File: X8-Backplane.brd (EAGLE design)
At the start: 122.1 x 89 mm, 18 parts, among them U1 BD6221FSOP, U2 MIC29501-5.0WU, U3 MIC29501-5.0WU, U4 FQB27P06, U5 FQB27P06, U6 FQB27P06

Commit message: added buck regulator
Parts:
- removed C1, C7: 10uF, SparkFun-Passives:0603-CAP
- removed C5, C8: 0.1uF, SparkFun-Passives:0603-CAP
- removed R1, R2: 10k, SparkFun-Passives:0603-RES
- removed U2, U3: MIC29501-5.0WU, LDO:TO-263-5
- added C10, C6, C9: 150uF, PowerComponents:CTAN(7.30_4.30MM)
- added C11, C12, C13, C2: 10uF, PowerComponents:CTAN(7.30_4.30MM)
- added C3: 0.47uF, SparkFun-Capacitors:0805
- added C4: 0.01uF, SparkFun-Passives:0603-CAP
- added U$2: SWITCHMODE_SCHOTTKY, PowerComponents:DPAK-3
- added U$6: 15uH, DiscreteComponents:HCMA1305
- added U7: LM2678, PowerComponents:LM2678
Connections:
- removed net +5V_CAMERA_TUBE: C7.1, U$4.57, U$4.58, U$4.59, U$4.60, U3.4, U4.3, U5.3, U6.3
- removed net EN1: R1.1, U2.1
- removed net EN2: R2.1, U3.1
- new net N$18: C4.1, U7.3
- new net N$19: C4.2, U$2.P$4, U$6.P$1, U7.1
- net +12V: now also C11.+, C12.+, C13.+, C2.+, C3.1, U7.2; no longer C5.1, C8.1, R1.2, R2.2, U2.2, U3.2
- net +5V: now also C10.+, C6.+, C9.+, U$4.57, U$4.58, U$4.59, U$4.60, U$6.P$2, U4.3, U5.3, U6.3, U7.6; no longer C1.1, U2.4
- net GND: now also C10.-, C11.-, C12.-, C13.-, C2.-, C3.2, C6.-, C9.-, U$2.P$1, U$2.P$3, U7.4, U7.TAB; no longer C1.2, C5.2, C7.2, C8.2, U2.3, U2.6, U3.3, U3.6
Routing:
- net +5V_LASER: track 0.00 -> 46.4 mm
- net +5V: track 108.6 -> 94.8 mm, vias 0 -> 2
- net N$19: track 0.00 -> 4.33 mm, vias 0 -> 1
- net N$18: track 0.00 -> 3.85 mm, vias 0 -> 1
- net +12V: track 2.52 -> 0.00 mm
- net EN1: track 2.01 -> 0.00 mm
- net EN2: track 1.93 -> 0.00 mm
- added copper zone on layer 16, net +5V
- added copper zone on layer 16, net N$19
- removed copper zone on layer 16, net +5V_CAMERA_TUBE
- removed copper zone on layer 16, net +5V_LASER

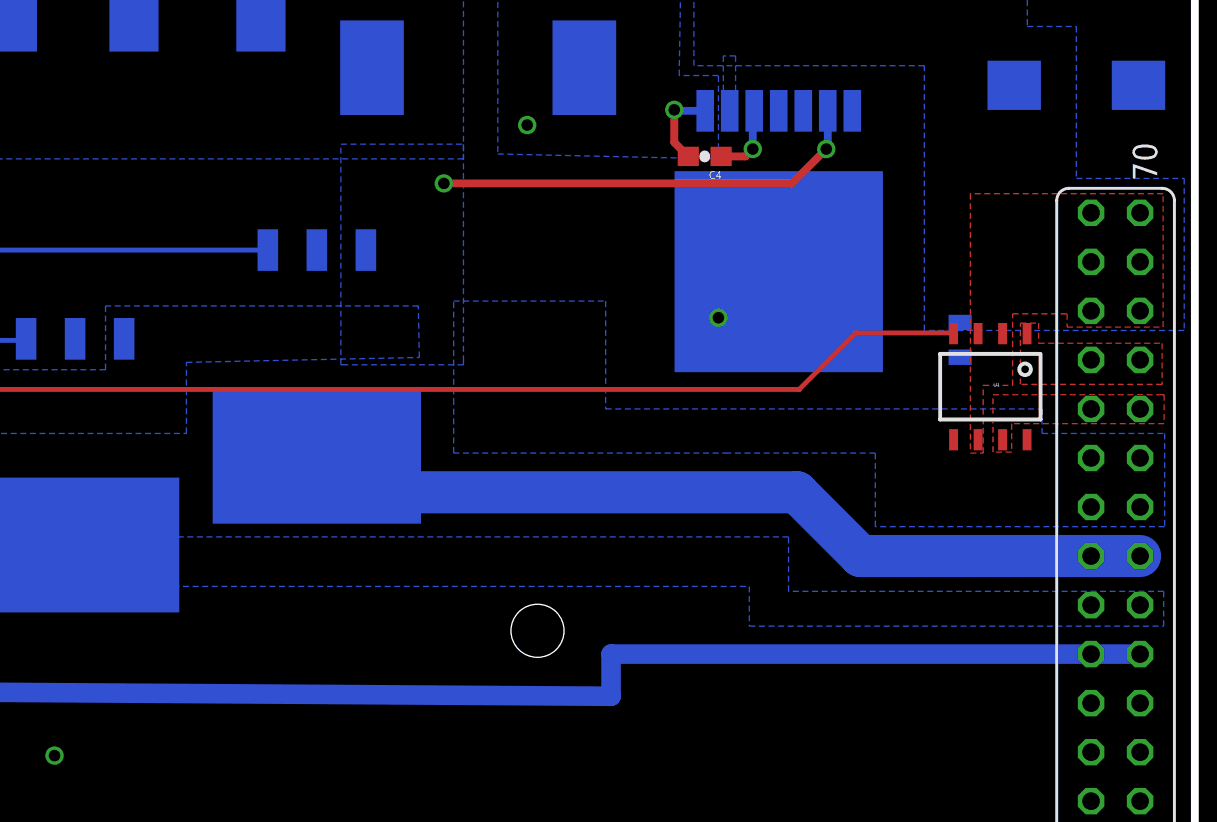
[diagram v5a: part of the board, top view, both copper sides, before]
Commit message: added more gnd vias
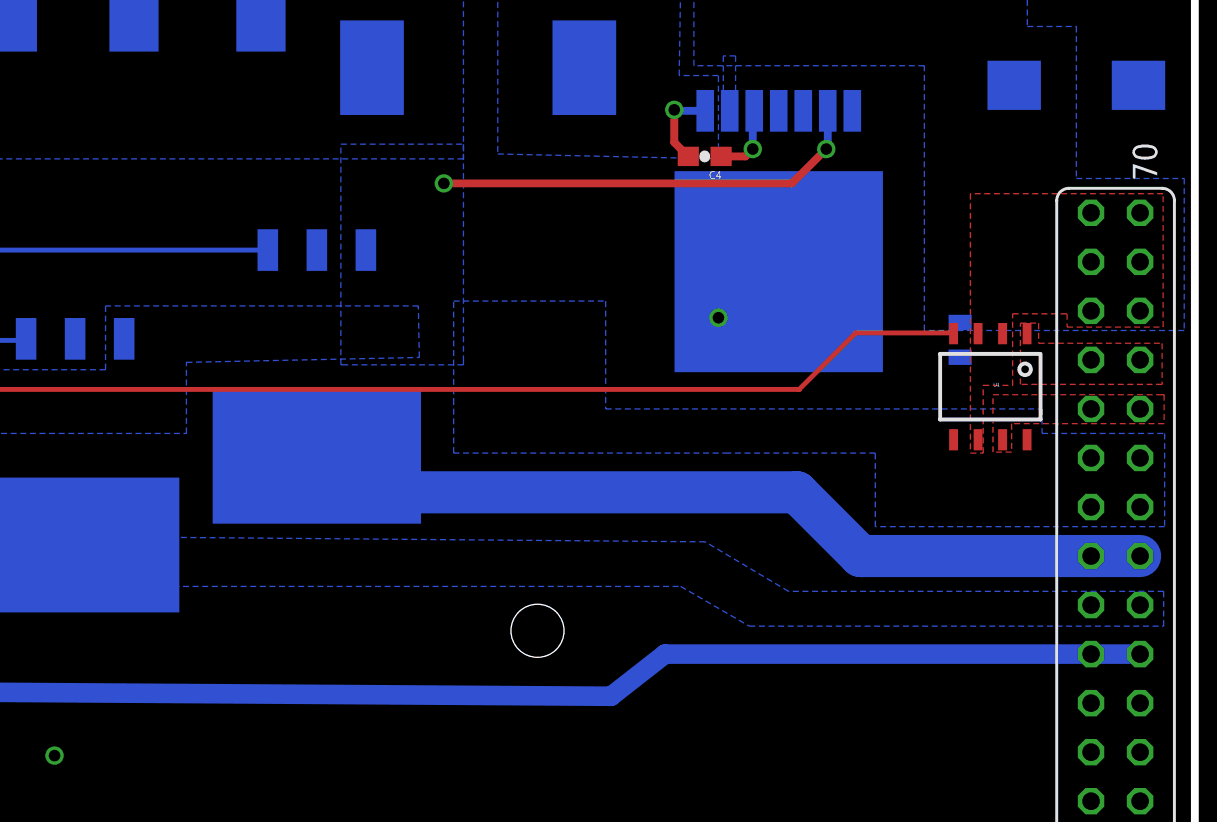
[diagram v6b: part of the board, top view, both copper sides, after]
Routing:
- net +5V_BT_LED: track 71.2 -> 69.7 mm
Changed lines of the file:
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@@
 <grid distance="10" unitdist="mil" unit="mil" style="lines" multiple="1" display="yes" altdistance="0.001" altunitdist="inch" altunit="inch"/>
 <layers>
-<layer number="1" name="Top" color="4" fill="1" visible="no" active="yes"/>
+<layer number="1" name="Top" color="4" fill="1" visible="yes" active="yes"/>
 <layer number="2" name="Route2" color="1" fill="3" visible="yes" active="yes"/>
 <layer number="3" name="Route3" color="4" fill="3" visible="no" active="yes"/>
@@
 <via x="47.1678" y="81.7626" extent="1-16" drill="0.6" diameter="0.3048"/>
 <via x="22.4028" y="64.0334" extent="1-16" drill="0.6" diameter="0.3048"/>
+<via x="32.385" y="35.433" extent="1-16" drill="0.6" diameter="0.3048"/>
+<via x="65.4304" y="21.6662" extent="1-16" drill="0.6" diameter="0.3048"/>
+<via x="102.9462" y="12.0396" extent="1-16" drill="0.6" diameter="0.3048"/>
+<via x="53.2638" y="57.9374" extent="1-16" drill="0.6" diameter="0.3048"/>
+<via x="49.2252" y="66.3194" extent="1-16" drill="0.6" diameter="0.3048"/>
+<via x="79.5782" y="79.0194" extent="1-16" drill="0.6" diameter="0.3048"/>
+<via x="102.743" y="77.1652" extent="1-16" drill="0.6" diameter="0.3048"/>
 </signal>
 <signal name="+12V">
@@
 <vertex x="122.8852" y="30.1752"/>
 <vertex x="103.4542" y="30.1752"/>
-<vertex x="103.4542" y="32.9946"/>
+<vertex x="99.1362" y="32.7406"/>
 <vertex x="68.6054" y="32.9946"/>
 <vertex x="68.6054" y="30.4292"/>
-<vertex x="101.4222" y="30.4292"/>
+<vertex x="97.8662" y="30.4292"/>
 <vertex x="101.4222" y="28.3718"/>
 <vertex x="122.8852" y="28.3718"/>
@@
 <contactref element="U$4" pad="52"/>
 <wire x1="119.126" y1="26.924" x2="121.666" y2="26.924" width="1.016" layer="16"/>
-<wire x1="119.126" y1="26.924" x2="94.2594" y2="26.924" width="1.016" layer="16"/>
-<wire x1="94.2594" y1="26.924" x2="94.2594" y2="24.7396" width="1.016" layer="16"/>
+<wire x1="119.126" y1="26.924" x2="97.0534" y2="26.924" width="1.016" layer="16"/>
+<wire x1="97.0534" y1="26.924" x2="94.2594" y2="24.7396" width="1.016" layer="16"/>
 <wire x1="94.2594" y1="24.7396" x2="54.6608" y2="24.9936" width="1.016" layer="16"/>
 <wire x1="54.6608" y1="24.9936" x2="54.4068" y2="26.9367" width="1.016" layer="16"/>
@@
 <via x="32.9946" y="12.5222" extent="1-16" drill="0.6" diameter="0.3048"/>
 </signal>
-<signal name="N$4">
-<via x="53.2638" y="57.9374" extent="1-16" drill="0.6" diameter="0.3048"/>
-</signal>
-<signal name="N$5">
-<via x="49.2252" y="66.3194" extent="1-16" drill="0.6" diameter="0.3048"/>
-</signal>
-<signal name="N$6">
-<via x="79.5782" y="79.0194" extent="1-16" drill="0.6" diameter="0.3048"/>
-</signal>
-<signal name="N$7">
-<via x="102.743" y="77.1652" extent="1-16" drill="0.6" diameter="0.3048"/>
-</signal>
 <signal name="N$8">
 <via x="65.2018" y="95.4786" extent="1-16" drill="0.6" diameter="0.3048"/>
@@
 <via x="18.923" y="12.2936" extent="1-16" drill="0.6" diameter="0.3048"/>
 </signal>
-<signal name="N$12">
-<via x="32.385" y="35.433" extent="1-16" drill="0.6" diameter="0.3048"/>
-</signal>
-<signal name="N$13">
-<via x="102.9462" y="12.0396" extent="1-16" drill="0.6" diameter="0.3048"/>
-</signal>
-<signal name="N$14">
-<via x="89.916" y="54.3306" extent="1-16" drill="0.6" diameter="0.3048"/>
-</signal>
 <signal name="N$15">
 <via x="99.822" y="44.3484" extent="1-16" drill="0.6" diameter="0.3048"/>
 </signal>
-<signal name="N$17">
-<via x="65.4304" y="21.6662" extent="1-16" drill="0.6" diameter="0.3048"/>
-</signal>
 <signal name="RX_H">

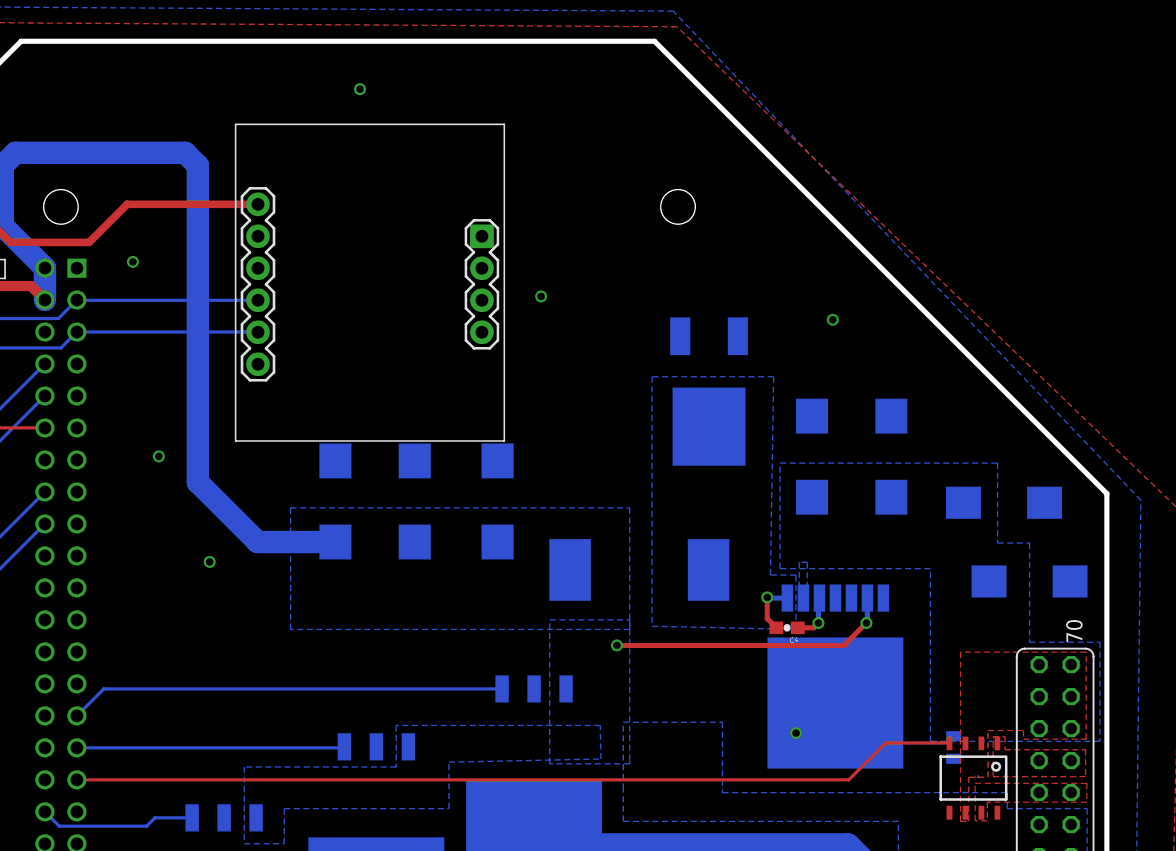
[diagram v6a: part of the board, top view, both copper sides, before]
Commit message: Moved the buck regulator parts
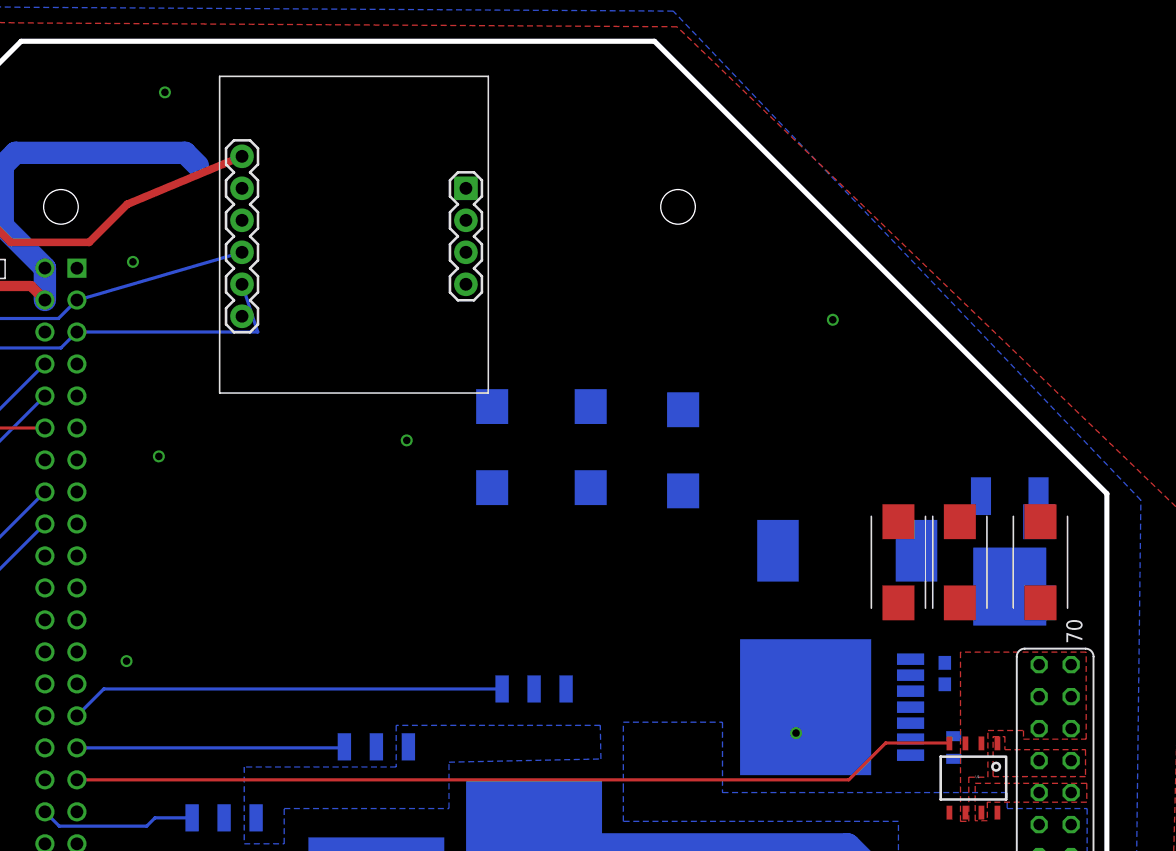
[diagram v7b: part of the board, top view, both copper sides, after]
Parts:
- moved U$2 27.0 mm to (116.8, 59.1)
- moved U$6 16.6 mm to (103.9, 58.8)
- moved C9 15.3 mm to (90.9, 66.8)
- moved C6 14.6 mm to (83.5, 67.1)
- moved C10 13.2 mm to (75.7, 67.1)
- moved C4 13.0 mm to (111.6, 49.1), flipped to the bottom, turned to 90 degrees
- moved C13 10.8 mm to (108.0, 57.9), flipped to the top
- moved C11 9.99 mm to (112.8, 57.9), flipped to the top
- moved C12 5.54 mm to (119.2, 57.9), flipped to the top, turned to 90 degrees
- moved U$3 4.02 mm to (64.7, 85.1)
- moved U7 2.39 mm to (100.6, 46.4), turned to 180 degrees
- moved C2 1.70 mm to (119.1, 57.9), turned to 90 degrees
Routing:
- net +5V: track 94.8 -> 34.0 mm, vias 2 -> 0
- net N$19: track 4.33 -> 0.00 mm, vias 1 -> 0
- net SCL: track 61.6 -> 65.6 mm
- net N$18: track 3.85 -> 0.00 mm, vias 1 -> 0
- net SDA: track 61.5 -> 60.8 mm
- net 3.3V: track 87.5 -> 87.0 mm
- removed copper zone on layer 16, net +12V
- removed copper zone on layer 16, net N$19

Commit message: To be reviewed
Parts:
- moved C4 3.93 mm to (108.9, 51.9), turned to 180 degrees
- moved U$3 3.81 mm to (64.7, 81.3)
- moved U$2 2.29 mm to (114.5, 59.1)
- moved C2 1.80 mm to (120.9, 57.7)
- moved C12 1.78 mm to (117.4, 57.9)
- moved C3 1.13 mm to (111.8, 44.2)
- moved C13 0.76 mm to (107.2, 57.9)
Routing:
- net +5V: track 34.0 -> 210.1 mm
- net +12V: track 0.00 -> 39.0 mm
- net N$19: track 0.00 -> 17.2 mm
- net N$18: track 0.00 -> 6.51 mm
- net SCL: track 65.6 -> 60.3 mm
- net 3.3V: track 87.0 -> 86.2 mm
- net SDA: track 60.8 -> 60.3 mm
